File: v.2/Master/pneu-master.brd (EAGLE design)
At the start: 61 x 50.8 mm, 68 parts, among them T1 FDN340P/PMV48XP, T2 PMV48XP, U2 NCP1117-5, Y2 16MHz

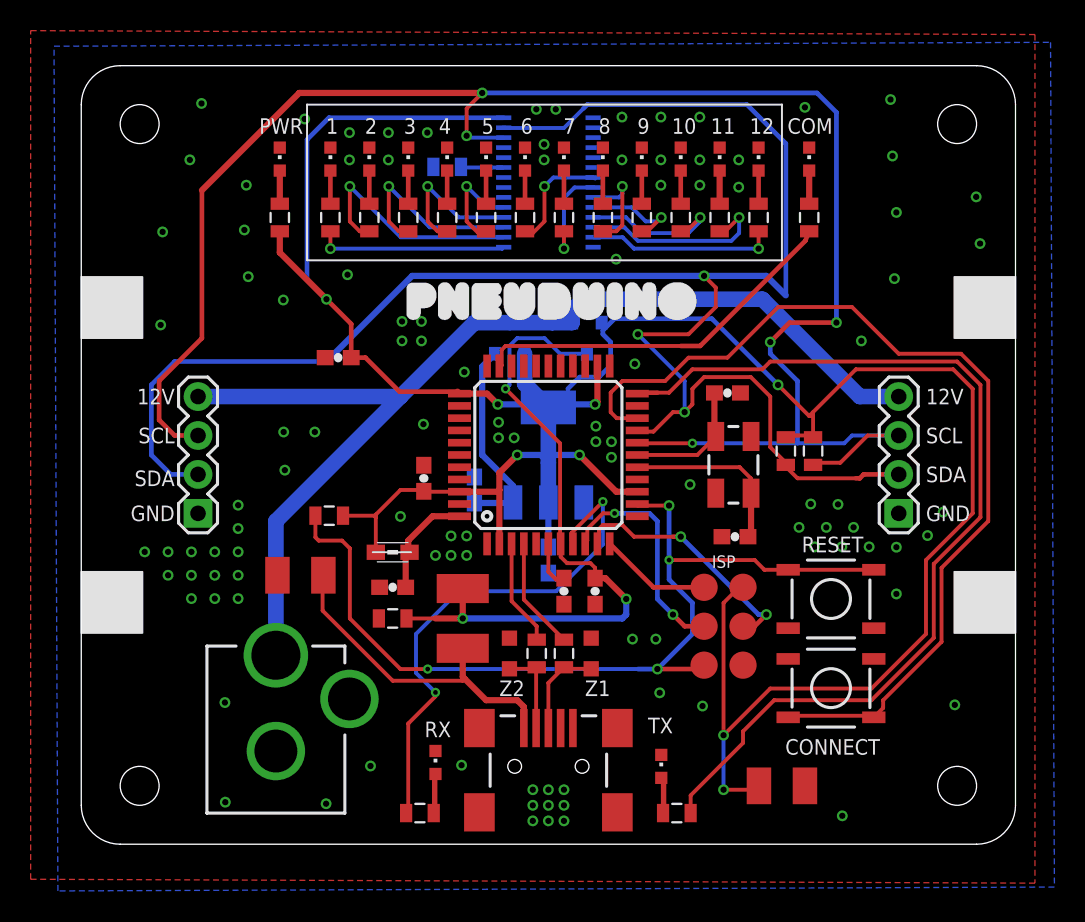
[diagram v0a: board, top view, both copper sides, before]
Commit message: minor changes
getting ready for production:

correct indicator led position on master board
add corner drills to slave boards
generate silk screens
adjust edge connector distance for better fit
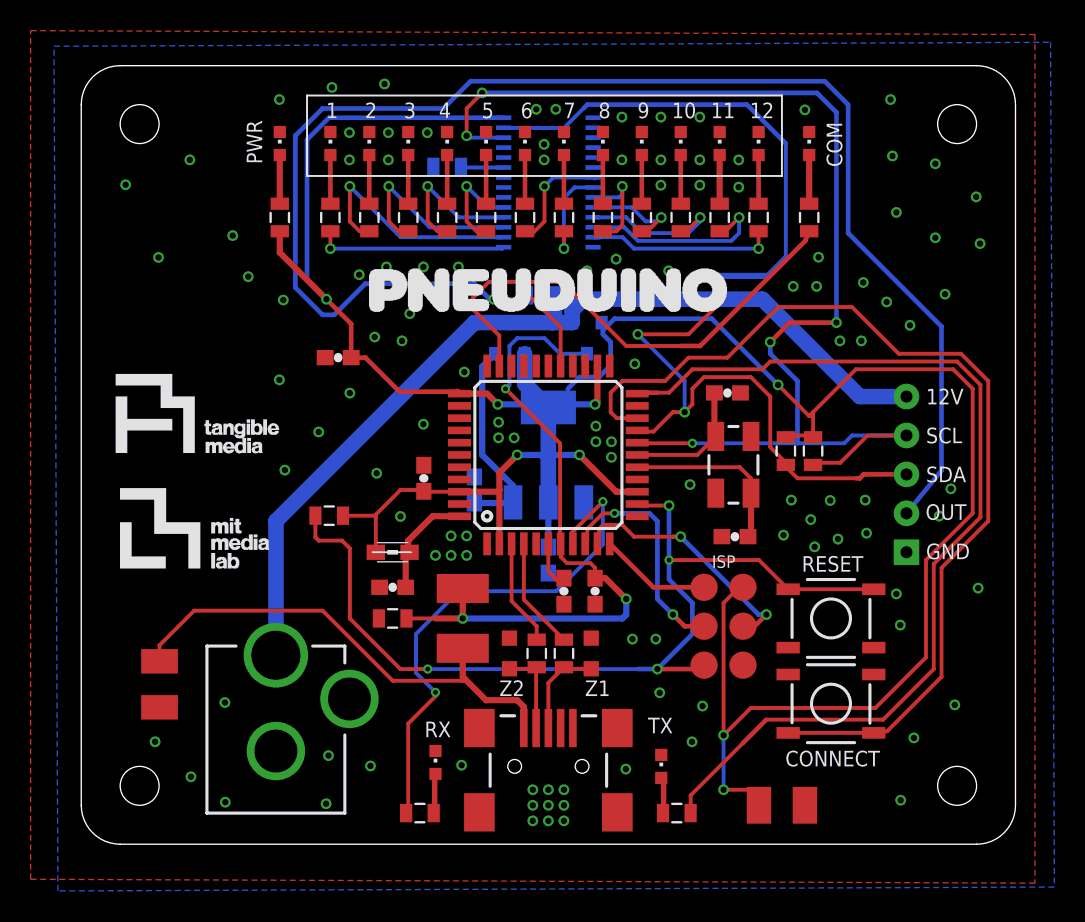
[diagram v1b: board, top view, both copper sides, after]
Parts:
- removed JP1, JP2: (no value), SparkFun-Connectors:1X04
- added U$14: 1X05, digikey:1X05_TIGHT
- moved C14 11.6 mm to (0.03, 10.4), turned to 270 degrees
- moved C3 1.27 mm to (40.6, 2.54)
- moved S1 1.27 mm to (43.8, 14.7)
- moved S2 1.02 mm to (43.8, 9.17)
- moved 1 1.02 mm to (11.2, 45.7)
- moved 10 1.02 mm to (34.0, 45.7)
- moved 11 1.02 mm to (36.6, 45.7)
- moved 12 1.02 mm to (39.1, 45.7)
- moved 2 1.02 mm to (13.7, 45.7)
- moved 3 1.02 mm to (16.3, 45.7)
- moved 4 1.02 mm to (18.8, 45.7)
- moved 5 1.02 mm to (21.3, 45.7)
- moved 6 1.02 mm to (23.9, 45.7)
- moved 7 1.02 mm to (26.4, 45.7)
- moved 8 1.02 mm to (29.0, 45.7)
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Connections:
- new net DATA_OUT: U$14.P$4, U$4.27
- net GND: now also U$14.P$5; no longer JP1.1, JP2.1
- net SCL: now also U$14.P$3; no longer JP1.3, JP2.3
- net SDA: now also U$14.P$2; no longer JP1.2, JP2.2
- net VIN: now also U$14.P$1; no longer JP1.4, JP2.4
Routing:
- net DATA_OUT: track 0.00 -> 100.7 mm, vias 0 -> 1
- net SDA: track 121.6 -> 72.4 mm
- net SCL: track 119.0 -> 80.0 mm
- net VIN: track 73.5 -> 60.8 mm
- net VUSBD: track 21.6 -> 31.9 mm
- net D13: track 24.9 -> 32.8 mm
- net +5V: track 187.2 -> 188.8 mm
- net N$9: track 2.16 -> 3.18 mm
- net N$25: track 2.16 -> 3.18 mm
- net N$24: track 2.16 -> 3.18 mm
- net N$23: track 2.16 -> 3.18 mm
- net N$22: track 2.16 -> 3.18 mm
- net N$21: track 2.16 -> 3.18 mm
- net N$20: track 2.16 -> 3.18 mm
- net N$19: track 2.16 -> 3.18 mm
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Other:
- board text added: "07/17/2016"
- board text added: "OUT"
- board text removed: "06/24/2015"
